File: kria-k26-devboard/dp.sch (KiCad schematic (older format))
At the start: 25 parts, among them J1 47272-0001, U1 74AVC4T245RSVRG4, U2 FIN1019MTC, U3 TPD4E05U06QDQARQ1, U4 WE-TVS-824012823

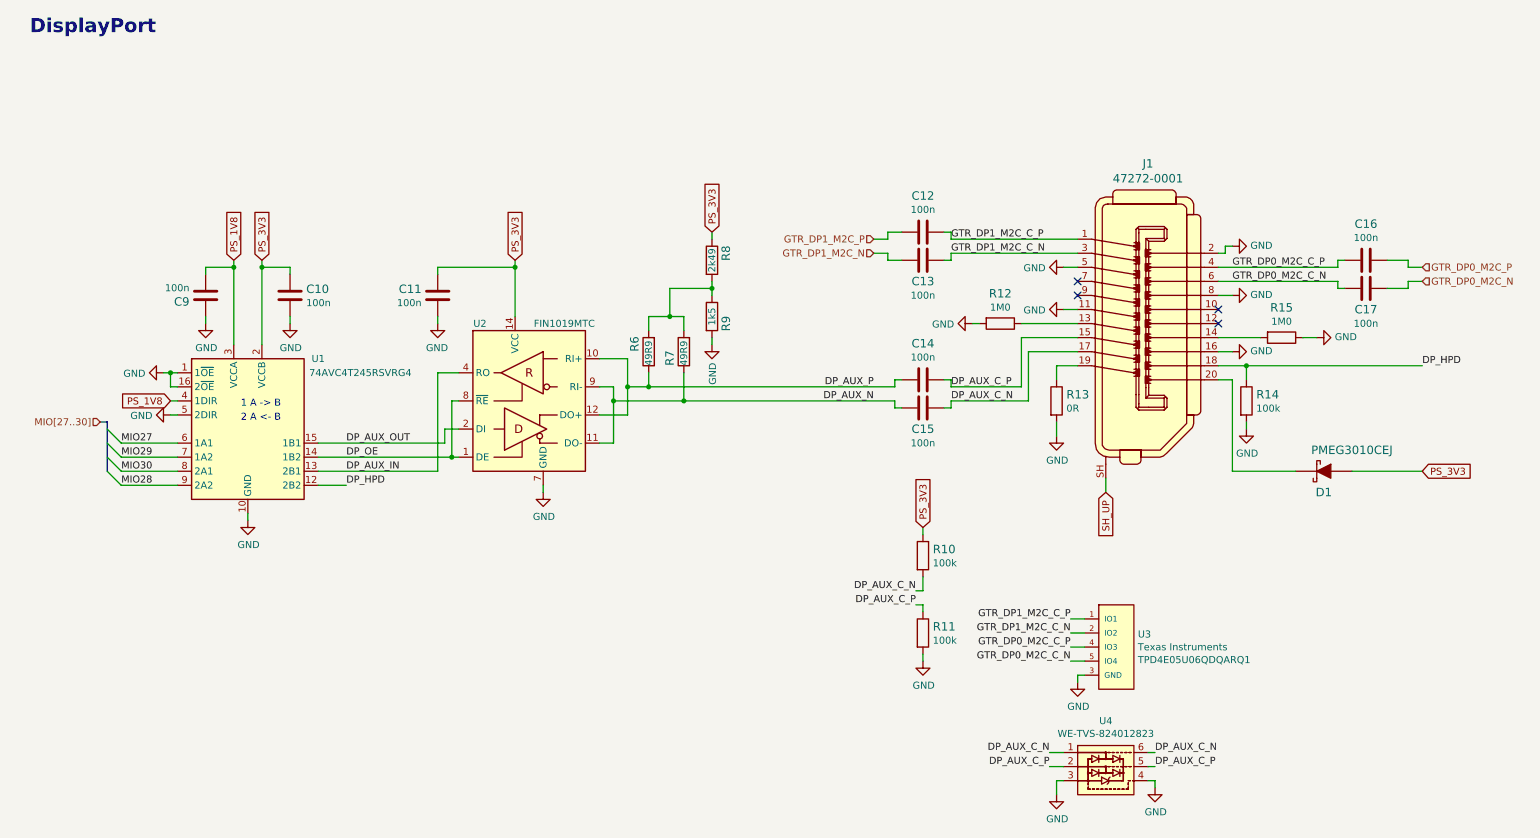
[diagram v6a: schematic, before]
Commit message: Modified TPD4E05U06QDQARQ1 symbol to avoid misconnections on the schematic
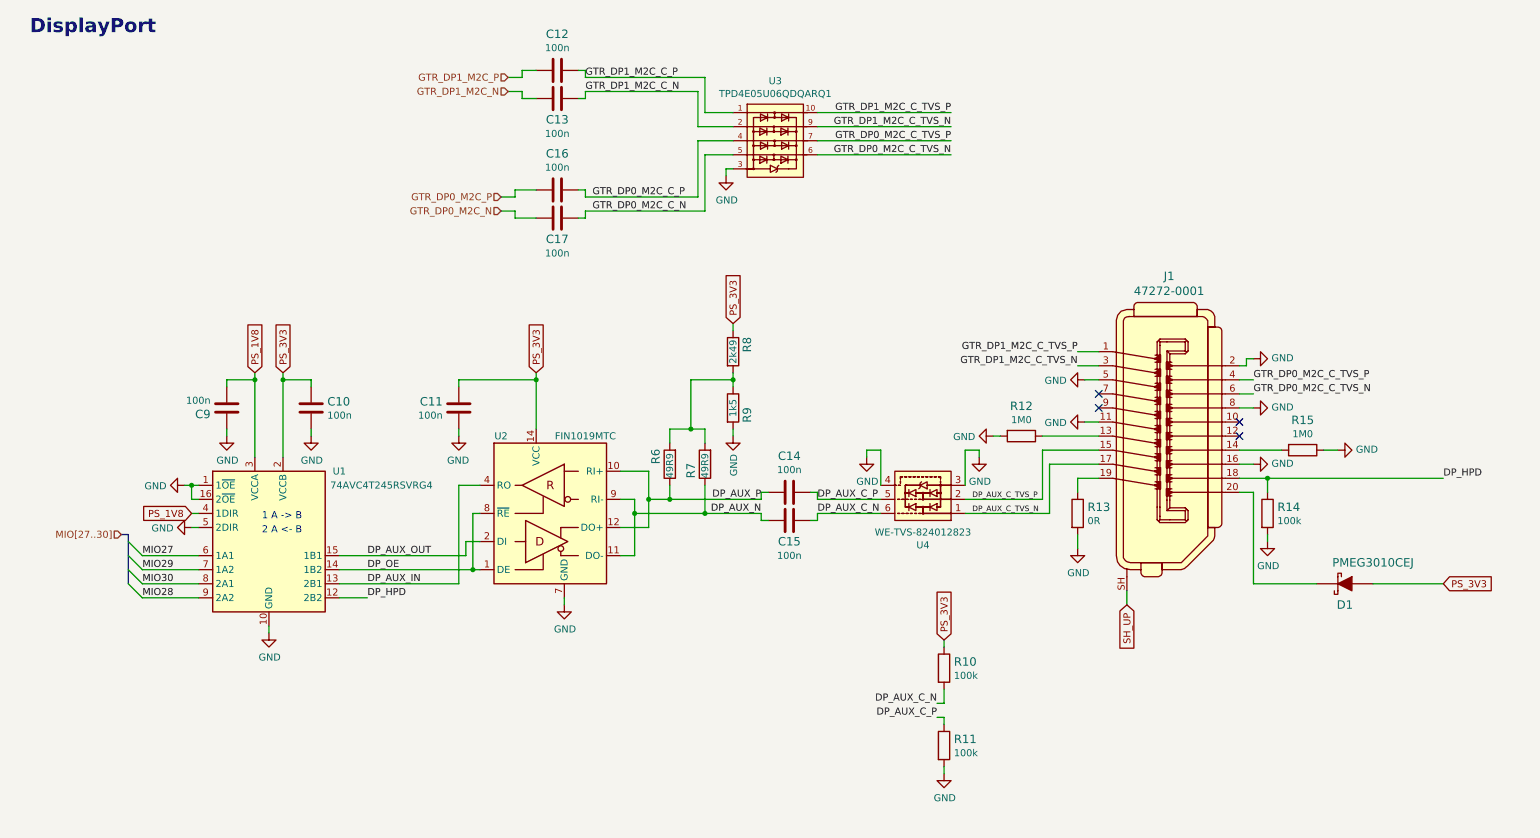
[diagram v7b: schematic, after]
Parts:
- removed U3: TPD4E05U06QDQARQ1, antmicro-footprints:TPD4E05U06QDQARQ1, symbol antmicroTVSDiodes:TPD4E05U06QDQARQ1
- added U3: TPD4E05U06QDQARQ1_PASS, antmicro-footprints:TPD4E05U06QDQARQ1, symbol antmicroTVSDiodes:TPD4E05U06QDQARQ1_PASS
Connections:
- net DP_AUX_C_N: no longer J1.17, U4.1
- net DP_AUX_C_P: no longer J1.15, U4.2
- net GND: now also U3.3, U3.8 (GND)
- net GTR_DP0_M2C_C_N: now also U3.5; no longer J1.6
- net GTR_DP0_M2C_C_P: now also U3.4; no longer J1.4
- net GTR_DP1_M2C_C_N: now also U3.2; no longer J1.3
- net GTR_DP1_M2C_C_P: now also U3.1; no longer J1.1
- new net DP_AUX_C_TVS_N: J1.17, U4.1
- new net DP_AUX_C_TVS_P: J1.15, U4.2
- new net GTR_DP0_M2C_C_TVS_N: J1.6, U3.6
- new net GTR_DP0_M2C_C_TVS_P: J1.4, U3.7
- new net GTR_DP1_M2C_C_TVS_N: J1.3, U3.9
- new net GTR_DP1_M2C_C_TVS_P: J1.1, U3.10
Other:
- moved on the sheet: C10, C11, C12, C13, C14, C15, C16, C17, C9, D1, J1, R10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
